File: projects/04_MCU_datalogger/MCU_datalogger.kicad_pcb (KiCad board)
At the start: 2 copper layers, 50.8 x 35.5 mm, 33 parts, among them J1 Conn_01x04_Pin, J2 Conn_01x09_Pin, J3 Conn_01x04_Pin, J4 Conn_02x03_Odd_Even, U1 24LC1025, U2 DS1337S_, U3 24LC1025, U4 ATMEGA328P-AU, Y1 32.768KHz, Y2 16MHz

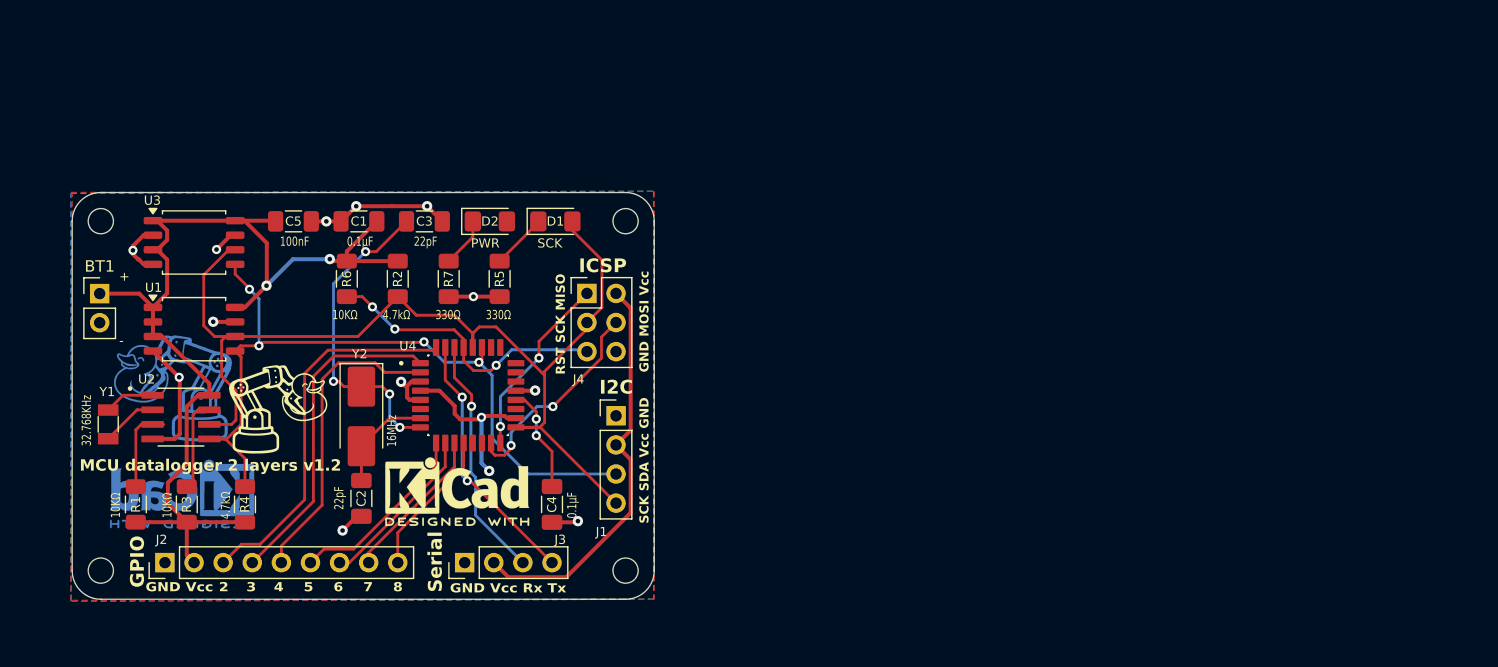
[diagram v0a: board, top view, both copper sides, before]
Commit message: MCU datalogger - clean up schematic
In `MCU_datalogger.kicad_sch` and `connectors.kicad_sch`:
- update RTC, EEPROM, Crystal symbols to arrange pins properly
  and align to 100 mil grid
- clean up schematic
- rename nets to start with ICSP_* I2C_* UART_*
- replace Vcc label with VCC power symbol
- add net colors

In `MCU_datalogger.kicad_pcb`:
- replace layout in main branch with empty placeholder referring to 2layer and 4layer branches

Notes:
- ensure modified symbols are saved in custom library (e.g. MH_library)
- before deleting the layout DRC threw hundreds of errors: unconnected pins, solder mask bridges, etc. (WHY?)
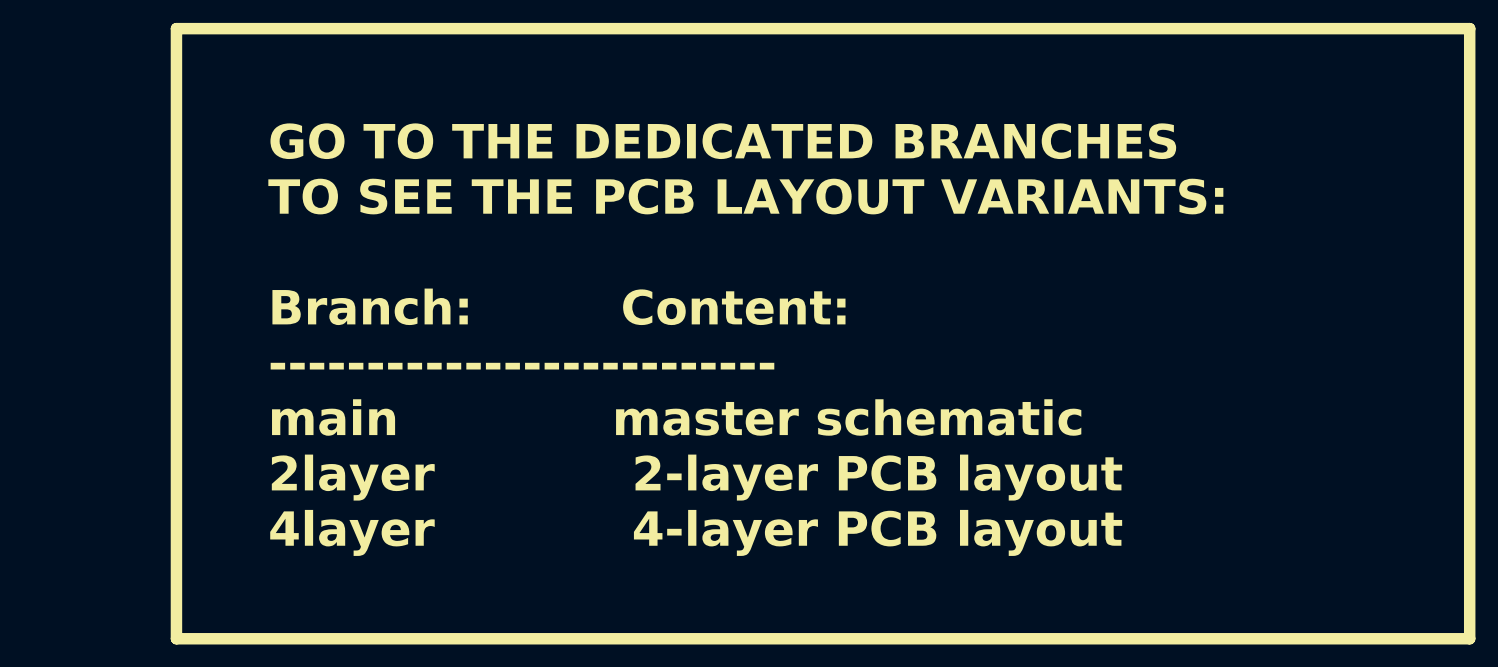
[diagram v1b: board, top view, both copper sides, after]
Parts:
- removed BT1: Battery, Connector_PinHeader_2.54mm:PinHeader_1x02_P2.54mm_Vertical
- removed C1, C4: 0.1μF, Capacitor_SMD:C_1206_3216Metric_Pad1.33x1.80mm_HandSolder
- removed C2, C3: 22pF, Capacitor_SMD:C_1206_3216Metric_Pad1.33x1.80mm_HandSolder
- removed C5: 100nF, Capacitor_SMD:C_1206_3216Metric_Pad1.33x1.80mm_HandSolder
- removed D1, D2: LED, LED_SMD:LED_1206_3216Metric_Pad1.42x1.75mm_HandSolder
- removed G***: LOGO, MH_LOGO:robot_duckie_logo_10mm
- removed G***: LOGO, MH_LOGO:robot_duckie_logo_12mm
- removed H1, H2, H3, H4: MountingHole, MountingHole:MountingHole_2.2mm_M2
- removed J1, J3: Conn_01x04_Pin, Connector_PinHeader_2.54mm:PinHeader_1x04_P2.54mm_Vertical
- removed J2: Conn_01x09_Pin, Connector_PinHeader_2.54mm:PinHeader_1x09_P2.54mm_Vertical
- removed J4: Conn_02x03_Odd_Even, Connector_PinHeader_2.54mm:PinHeader_2x03_P2.54mm_Vertical
- removed R1, R3, R6: 10KΩ, Resistor_SMD:R_1206_3216Metric_Pad1.30x1.75mm_HandSolder
- removed R2, R4: 4.7kΩ, Resistor_SMD:R_1206_3216Metric_Pad1.30x1.75mm_HandSolder
- removed R5, R7: 330Ω, Resistor_SMD:R_1206_3216Metric_Pad1.30x1.75mm_HandSolder
- removed REF**: KiCad-Logo2_5mm_SilkScreen, Symbol:KiCad-Logo2_5mm_SilkScreen
- removed REF**: KiCad-Logo2_5mm_Copper, Symbol:KiCad-Logo2_5mm_Copper
- removed U1, U3: 24LC1025, Package_SO:SOIC-8_5.3x5.3mm_P1.27mm
- removed U2: DS1337S_, MH_DS1337S:SOIC127P600X175-8N
- removed U4: ATMEGA328P-AU, MH_ATMEGA328:QFP80P900X900X120-32N
- removed Y1: 32.768KHz, Crystal:Crystal_SMD_3215-2Pin_3.2x1.5mm
- removed Y2: 16MHz, Crystal:Crystal_SMD_5032-2Pin_5.0x3.2mm_HandSoldering
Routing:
- net /Vcc: track 141.5 -> 0.00 mm, vias 4 -> 0
- net /SCK: track 91.8 -> 0.00 mm
- net /SDA: track 65.2 -> 0.00 mm, vias 4 -> 0
- net GND: track 47.7 -> 0.00 mm, vias 12 -> 0
- net /D2: track 32.8 -> 0.00 mm
- net /D3: track 29.5 -> 0.00 mm
- net Net-(U4-PB7): track 27.8 -> 0.00 mm, vias 4 -> 0
- net /D4: track 27.0 -> 0.00 mm
- net /RESET: track 25.5 -> 0.00 mm, vias 3 -> 0
- net /TX: track 22.8 -> 0.00 mm, vias 2 -> 0
- net /RX: track 21.3 -> 0.00 mm, vias 1 -> 0
- net /MOSI: track 18.5 -> 0.00 mm, vias 2 -> 0
- net /D5: track 16.5 -> 0.00 mm
- net /MISO: track 16.2 -> 0.00 mm, vias 2 -> 0
- net /D6: track 14.8 -> 0.00 mm
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- removed copper zone on F.Cu, net /Vcc
- removed copper zone on B.Cu, net GND
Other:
- board outline removed
- board text added: "GO TO THE DEDICATED BRANCHES TO SEE THE PCB LAYOUT VARIANTS: Branch: Content: -------------------------- main master schematic 2layer 2-layer PCB layout 4layer 4-layer PCB layout"
- board text removed: "+"
- board text removed: "-"
- board text removed: "0.2000 mm / 0.0000 mm"
- board text removed: "0.3000 mm"
- board text removed: "1.6000 mm"
- board text removed: "2"
- board text removed: "2 Mbit EEPROM RTC I2C SPI GPIOs"
- board text removed: "3"
- board text removed: "4"
- board text removed: "5"
- board text removed: "50.8000 mm x 35.5000 mm"
- board text removed: "6"
- board text removed: "7"
- board text removed: "8"
- board text removed: "BOARD CHARACTERISTICS"
- board text removed: "Board Thickness:"
- board text removed: "Board overall dimensions:"
- board text removed: "Castellated pads:"
- board text removed: "Copper Finish:"
- board text removed: "Copper Layer Count:"
- board text removed: "Edge card connectors:"
- board text removed: "GND MOSI Vcc"
- board text removed: "GND Vcc"
- board text removed: "GND Vcc Rx Tx"
- board text removed: "GPIO"
- board text removed: "I2C"
- board text removed: "ICSP"
- board text removed: "Impedance Control:"
- board text removed: "MCU datalogger 2 layers v1.2"
- board text removed: "Min hole diameter:"
- board text removed: "Min track/spacing:"
- board text removed: "No"
- board text removed: "None"
- board text removed: "PWR"
- board text removed: "Plated Board Edge:"
- board text removed: "RST SCK MISO"
- board text removed: "SCK"
- board text removed: "SCK SDA Vcc GND"
- board text removed: "Serial"
